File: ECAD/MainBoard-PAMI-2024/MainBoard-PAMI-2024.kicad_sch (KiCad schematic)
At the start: 50 parts, among them J1 Selecteur-Robot, J10 Serial, J11 Con_Batt, J12 BAU, J13 OLED, J2 USB_B, J3 Tirette, J4 Servo, J5 Sensor_Right, J6 Sensor_Left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

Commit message: Silkscreen
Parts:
- added H3: MountingHole, MountingHole:MountingHole_3.2mm_M3, symbol Mechanical:MountingHole
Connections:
- net TX: now reaches J10.1 (Pin_1), U1.37 (U0TXD/GPIO43/CLK_OUT1)
- net RX: now reaches J10.2 (Pin_2), U1.36 (U0RXD/GPIO44/CLK_OUT2)
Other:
- moved on the sheet: H1, H2
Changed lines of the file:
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@@
     (effects (font (size 1.27 1.27)) (justify left bottom))
   )
+  (label "TX" (at 168.91 72.39 0) (fields_autoplaced)
+    (effects (font (size 1.27 1.27)) (justify left bottom))
+  )
+  (label "RX" (at 168.91 74.93 0) (fields_autoplaced)
+    (effects (font (size 1.27 1.27)) (justify left bottom))
+  )
   (global_label "EnDriver" (shape input) (at 167.64 143.51 0) (fields_autoplaced)
     (effects (font (size 1.27 1.27)) (justify left))
@@
     )
   )
-  (symbol (lib_id "Mechanical:MountingHole") (at 266.7 157.48 0) (unit 1)
+  (symbol (lib_id "Mechanical:MountingHole") (at 266.7 151.13 0) (unit 1)
     (in_bom yes) (on_board yes) (dnp no)
-    (property "Reference" "H1" (at 269.24 156.21 0)
-      (effects (font (size 1.27 1.27)) (justify left))
-    )
-    (property "Value" "MountingHole" (at 269.24 158.75 0)
-      (effects (font (size 1.27 1.27)) (justify left))
-    )
-    (property "Footprint" "MountingHole:MountingHole_3.2mm_M3" (at 266.7 157.48 0)
-      (effects (font (size 1.27 1.27)) hide)
-    )
-    (property "Datasheet" "~" (at 266.7 157.48 0)
+    (property "Reference" "H1" (at 269.24 149.86 0)
+      (effects (font (size 1.27 1.27)) (justify left))
+    )
+    (property "Value" "MountingHole" (at 269.24 152.4 0)
+      (effects (font (size 1.27 1.27)) (justify left))
+    )
+    (property "Footprint" "MountingHole:MountingHole_3.2mm_M3" (at 266.7 151.13 0)
+      (effects (font (size 1.27 1.27)) hide)
+    )
+    (property "Datasheet" "~" (at 266.7 151.13 0)
       (effects (font (size 1.27 1.27)) hide)
     )
@@
     )
   )
+  (symbol (lib_id "Mechanical:MountingHole") (at 266.7 161.29 0) (unit 1)
+    (in_bom yes) (on_board yes) (dnp no)
+    (property "Reference" "H3" (at 269.24 160.02 0)
+      (effects (font (size 1.27 1.27)) (justify left))
+    )
+    (property "Value" "MountingHole" (at 269.24 162.56 0)
+      (effects (font (size 1.27 1.27)) (justify left))
+    )
+    (property "Footprint" "MountingHole:MountingHole_3.2mm_M3" (at 266.7 161.29 0)
+      (effects (font (size 1.27 1.27)) hide)
+    )
+    (property "Datasheet" "~" (at 266.7 161.29 0)
+      (effects (font (size 1.27 1.27)) hide)
+    )
+    (instances
+      (project "MainBoard-PAMI-2024"
+        (path "/d3e1aeb6-1412-4438-ac7d-372534bf2609"
+          (reference "H3") (unit 1)
+        )
+      )
+    )
+  )
   (symbol (lib_id "Device:C_Polarized_Small") (at 63.5 34.29 0) (unit 1)
     (in_bom yes) (on_board yes) (dnp no) (fields_autoplaced)
@@
     )
   )
-  (symbol (lib_id "Mechanical:MountingHole") (at 266.7 162.56 0) (unit 1)
+  (symbol (lib_id "Mechanical:MountingHole") (at 266.7 156.21 0) (unit 1)
     (in_bom yes) (on_board yes) (dnp no)
-    (property "Reference" "H2" (at 269.24 161.29 0)
-      (effects (font (size 1.27 1.27)) (justify left))
-    )
-    (property "Value" "MountingHole" (at 269.24 163.83 0)
-      (effects (font (size 1.27 1.27)) (justify left))
-    )
-    (property "Footprint" "MountingHole:MountingHole_3.2mm_M3" (at 266.7 162.56 0)
-      (effects (font (size 1.27 1.27)) hide)
-    )
-    (property "Datasheet" "~" (at 266.7 162.56 0)
-      (effects (font (size 1.27 1.27)) hide)
-    )
+    (property "Reference" "H2" (at 269.24 154.94 0)
+      (effects (font (size 1.27 1.27)) (justify left))
+    )
+    (property "Value" "MountingHole" (at 269.24 157.48 0)
+      (effects (font (size 1.27 1.27)) (justify left))
+    )
+    (property "Footprint" "MountingHole:MountingHole_3.2mm_M3" (at 266.7 156.21 0)
+      (effects (font (size 1.27 1.27)) hide)
+    )
+    (property "Datasheet" "~" (at 266.7 156.21 0)
+      (effects (font (size 1.27 1.27)) hide)
+    )

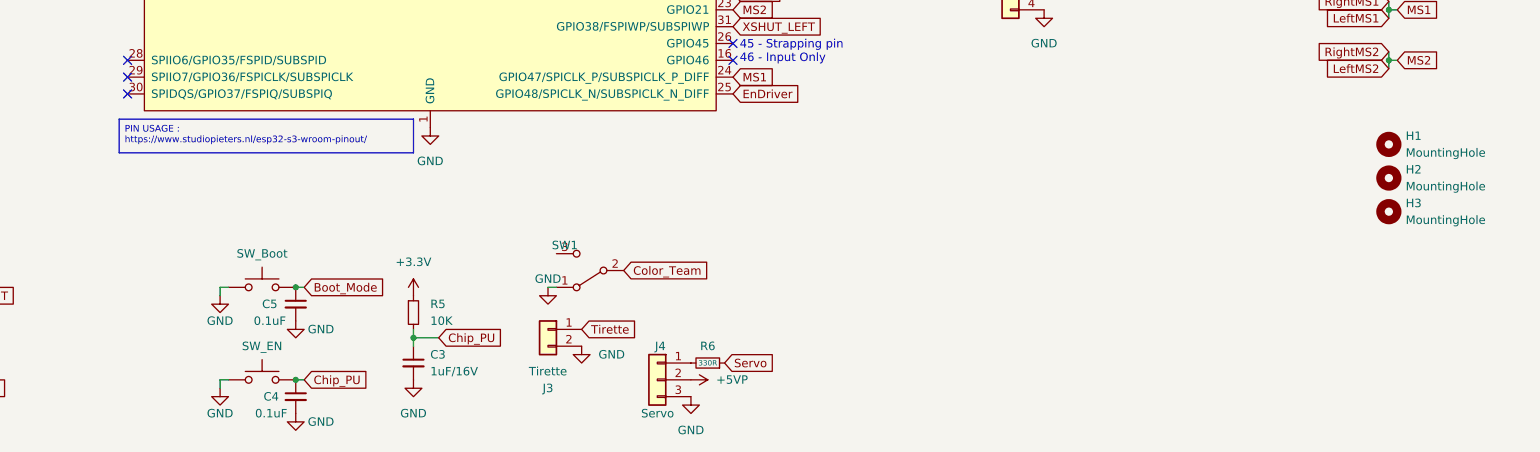
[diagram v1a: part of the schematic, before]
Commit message: add info on cap boot
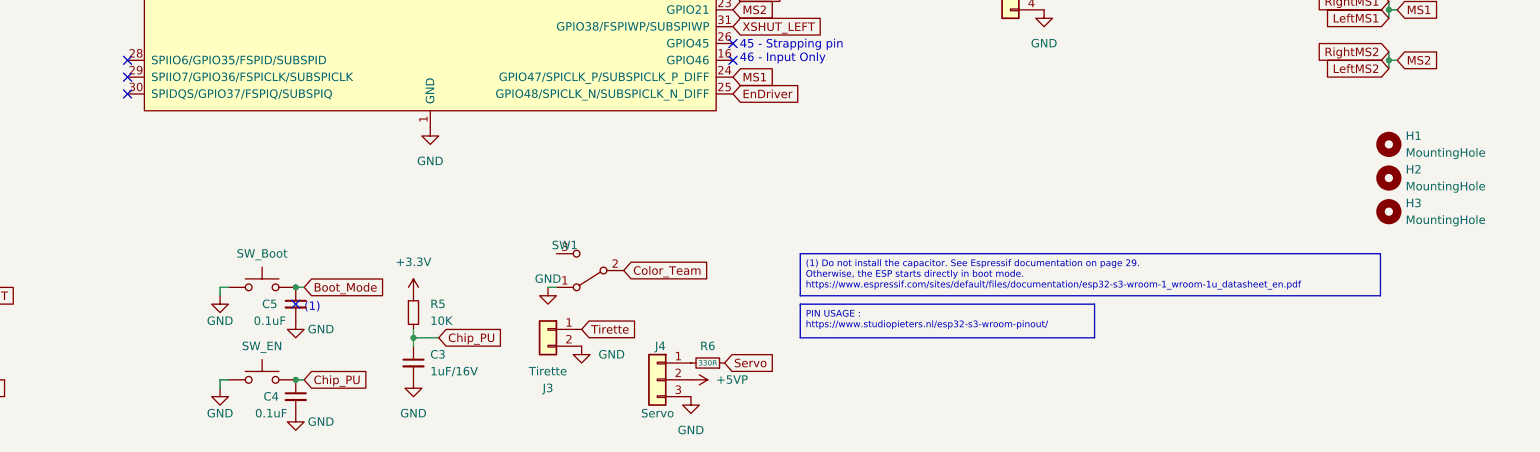
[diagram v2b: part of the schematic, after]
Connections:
- no-connect marks 21 -> 22
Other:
- note added: "(1)"
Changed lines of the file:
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@@
   (no_connect (at 271.78 105.41))
   (no_connect (at 76.2 138.43))
+  (no_connect (at 101.6 175.26))
   (no_connect (at 271.78 87.63))
   (no_connect (at 236.22 107.95))
@@
   )
   (text_box "PIN USAGE : https://www.studiopieters.nl/esp32-s3-wroom-pinout/"
-    (at 74.93 147.32 0) (size 44.45 5.08)
+    (at 177.8 175.26 0) (size 44.45 5.08)
     (stroke (width 0) (type default))
     (fill (type none))
@@
     (effects (font (size 1.27 1.27)) (justify left top))
   )
+  (text_box "(1) Do not install the capacitor. See Espressif documentation on page 29.\nOtherwise, the ESP starts directly in boot mode.\nhttps://www.espressif.com/sites/default/files/documentation/esp32-s3-wroom-1_wroom-1u_datasheet_en.pdf"
+    (at 177.8 167.64 0) (size 87.63 6.35)
+    (stroke (width 0) (type default))
+    (fill (type none))
+    (effects (font (size 1 1)) (justify left top))
+  )
   (text "Put near the \ntwo drivers\nTMC2208" (at 220.98 26.67 0)
     (effects (font (size 1.27 1.27)) (justify left bottom))
   )
+  (text "(1)" (at 102.87 176.53 0)
+    (effects (font (size 1.27 1.27)) (justify left bottom))
+  )
